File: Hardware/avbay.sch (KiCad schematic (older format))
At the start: 15 parts, among them P1 TERM_BLOCK_2.54MM_2POS, P2 CONN_6, P3 TERM_BLOCK_2.54MM_12POS, P4 TERM_BLOCK_2.54MM_2POS, P5 TERM_BLOCK_2.54MM_2POS, SW1 SW_PUSH, SW2 SW_PUSH

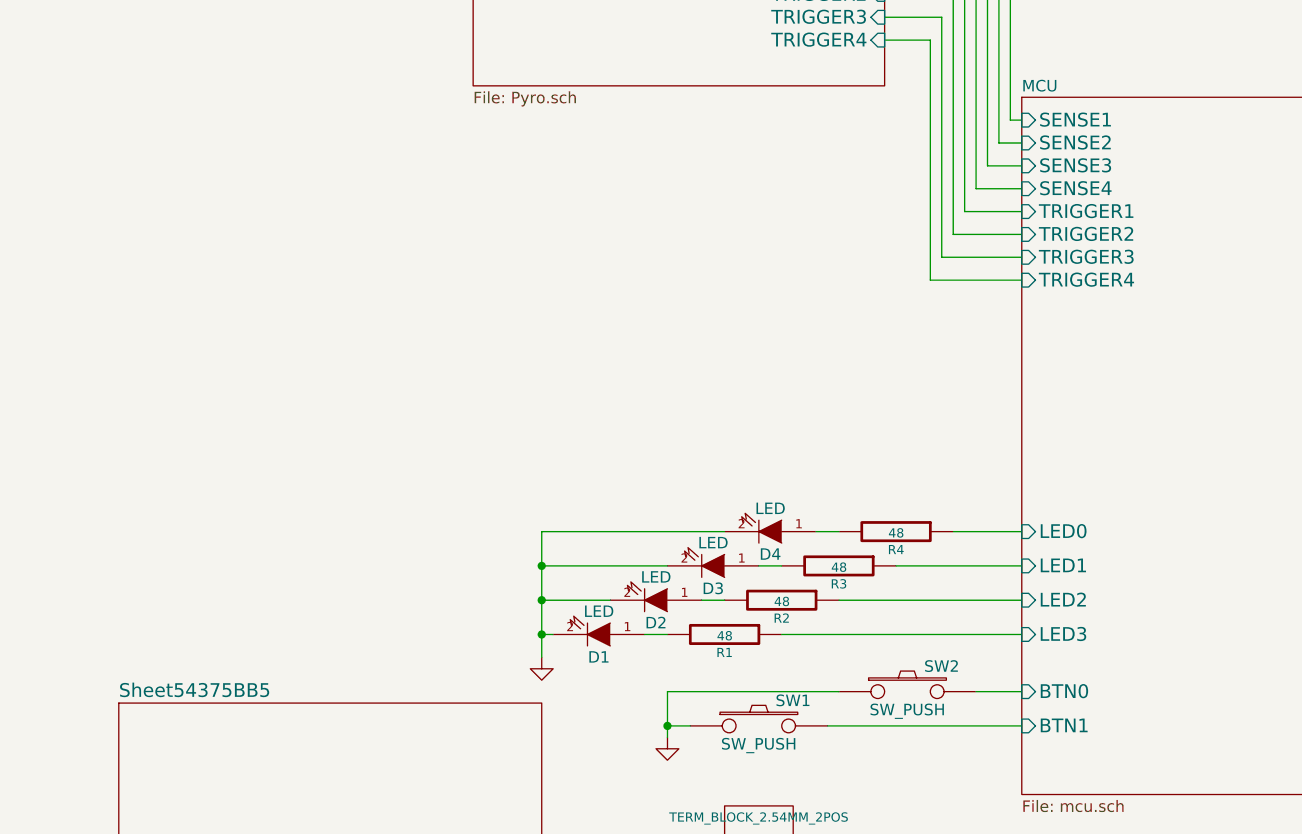
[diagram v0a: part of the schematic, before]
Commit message: Added sensors and sensor passives
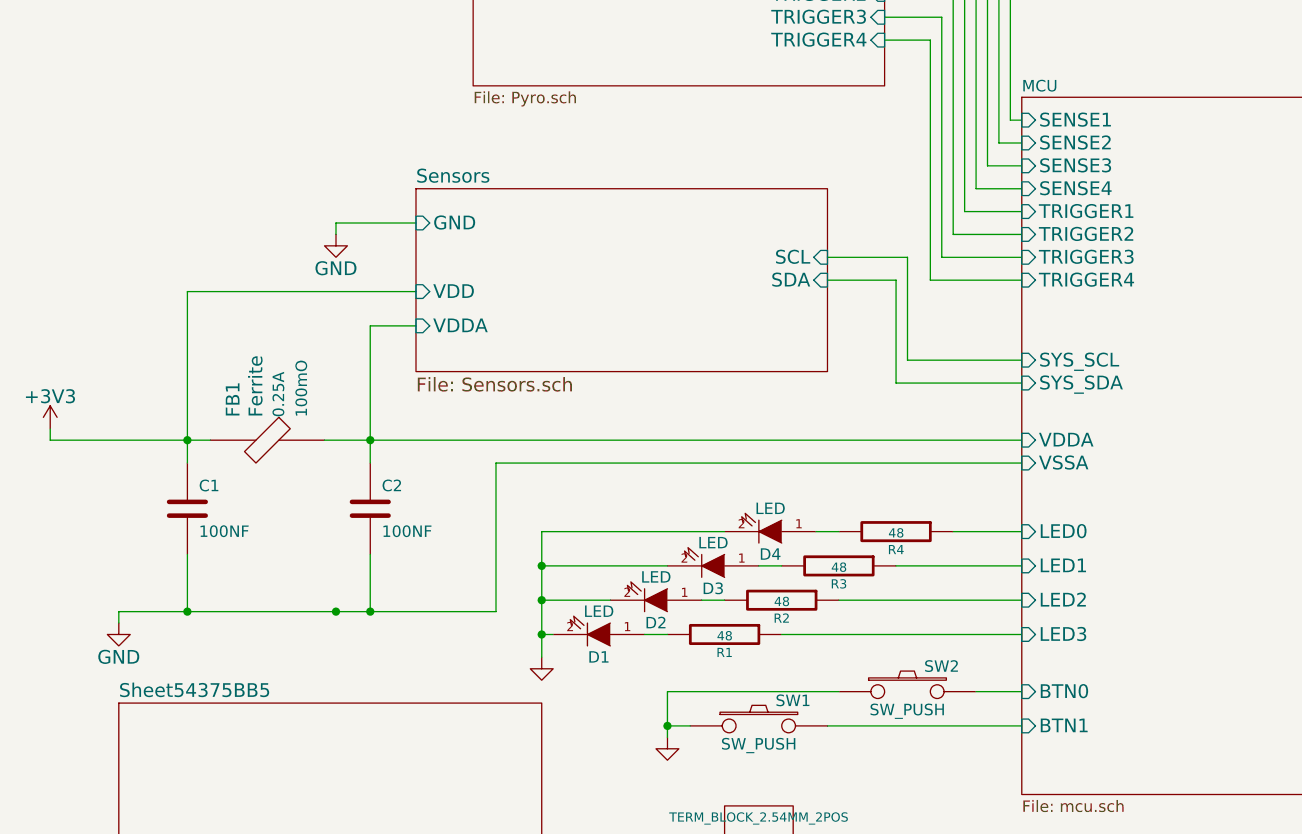
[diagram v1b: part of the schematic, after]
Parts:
- added C1, C2: 100NF, symbol C
- added FB1: Ferrite, symbol Ferrite
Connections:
- net labels added: +3V3
- wire segments 95 -> 116

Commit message: Roughed out PCB layout
Known issues:
- SW_PUSH holes too small. New footprint needed
- Sensor footprints are completely wrong.
- Regulator footprints might not be correct.

Tasks:
- Place passives according to schematic (especially
  with decoupling capacitors.
- Condense layout as much as possible for
  smallest board size
- Route board
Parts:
- removed P3: TERM_BLOCK_2.54MM_12POS, symbol TERM_BLOCK_2.54MM_12POS
- removed P4, P5: TERM_BLOCK_2.54MM_2POS, symbol TERM_BLOCK_2.54MM_2POS
- removed SW1: SW_PUSH, Discret:SW_PUSH_SMALL, symbol SW_PUSH
- added P3: TERM_BLOCK_2.54MM_8POS, Socket_Strips:Socket_Strip_Straight_1x08, symbol TERM_BLOCK_2.54MM_8POS
- added P4, P5: TERM_BLOCK_2.54MM_5POS, Socket_Strips:Socket_Strip_Straight_1x05, symbol TERM_BLOCK_2.54MM_5POS
- C1, C2: footprint (none) -> Capacitors_SMD:C_0805_HandSoldering
- FB1: footprint (none) -> SMD_Packages:SMD-1206
- P1: footprint (none) -> Socket_Strips:Socket_Strip_Straight_1x02
- P2: footprint Pin_Headers:Pin_Header_Angled_1x06 -> Socket_Strips:Socket_Strip_Angled_1x06
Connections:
- wire segments 116 -> 126
- no-connect marks 0 -> 4

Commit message: Began routing
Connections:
- no-connect marks 4 -> 5

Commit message: Finished routing.
Board awaiting review
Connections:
- net +3V3 is gone; now on net 3V3: C1.1, FB1.1, P3.5 (P5)
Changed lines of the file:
@@
-$EndComp
-$Comp
-L +3V3 #PWR09
-U 1 1 54C47AF6
-P 650 4050
-F 0 "#PWR09" H 650 3900 60  0001 C CNN
-F 1 "+3V3" H 650 4190 60  0000 C CNN
-F 2 "" H 650 4050 60  0000 C CNN
-F 3 "" H 650 4050 60  0000 C CNN
-	1    650  4050
-	1    0    0    -1
 $EndComp
 $Comp
@@
 $EndSheet
 $Comp
-L GND #PWR010
+L GND #PWR09
 U 1 1 54C502C9
 P 1900 3200
-F 0 "#PWR010" H 1900 2950 60  0001 C CNN
+F 0 "#PWR09" H 1900 2950 60  0001 C CNN
 F 1 "GND" H 1900 3050 60  0000 C CNN
 F 2 "" H 1900 3200 60  0000 C CNN
@@
 $EndComp
 $Comp
-L GND #PWR011
+L GND #PWR010
 U 1 1 5437EF10
 P 9200 5050
-F 0 "#PWR011" H 9200 5050 30  0001 C CNN
+F 0 "#PWR010" H 9200 5050 30  0001 C CNN
 F 1 "GND" H 9200 4980 30  0001 C CNN
 F 2 "" H 9200 5050 60  0000 C CNN
@@
 $EndComp
 $Comp
-L +3V3 #PWR012
-U 1 1 54C4EBE1
-P 7600 5700
-F 0 "#PWR012" H 7600 5550 60  0001 C CNN
-F 1 "+3V3" H 7600 5840 60  0000 C CNN
-F 2 "" H 7600 5700 60  0000 C CNN
-F 3 "" H 7600 5700 60  0000 C CNN
-	1    7600 5700
-	1    0    0    -1
-$EndComp
-$Comp
-L +5V #PWR013
+L +5V #PWR011
 U 1 1 54C4EC96
 P 7700 5700
-F 0 "#PWR013" H 7700 5550 60  0001 C CNN
+F 0 "#PWR011" H 7700 5550 60  0001 C CNN
 F 1 "+5V" H 7700 5840 60  0000 C CNN
 F 2 "" H 7700 5700 60  0000 C CNN
@@
 $EndComp
 $Comp
-L GND #PWR014
+L GND #PWR012
 U 1 1 54C501F1
 P 8300 5800
-F 0 "#PWR014" H 8300 5800 30  0001 C CNN
+F 0 "#PWR012" H 8300 5800 30  0001 C CNN
 F 1 "GND" H 8300 5730 30  0001 C CNN
 F 2 "" H 8300 5800 60  0000 C CNN
@@
 $EndComp
 $Comp
-L PWR_FLAG #FLG015
+L PWR_FLAG #FLG013
 U 1 1 54CB18F4
 P 3200 6300
-F 0 "#FLG015" H 3200 6395 30  0001 C CNN
+F 0 "#FLG013" H 3200 6395 30  0001 C CNN
 F 1 "PWR_FLAG" H 3200 6480 30  0000 C CNN
 F 2 "" H 3200 6300 60  0000 C CNN
@@
 $EndComp
 $Comp
-L PWR_FLAG #FLG016
+L PWR_FLAG #FLG014
 U 1 1 54CB23F4
 P 1900 4100
-F 0 "#FLG016" H 1900 4195 30  0001 C CNN
+F 0 "#FLG014" H 1900 4195 30  0001 C CNN
 F 1 "PWR_FLAG" H 1900 4280 30  0000 C CNN
 F 2 "" H 1900 4100 60  0000 C CNN
@@
 Connection ~ 3200 6300
 $Comp
-L PWR_FLAG #FLG017
+L PWR_FLAG #FLG015
 U 1 1 54CB3533
 P 4200 6300
-F 0 "#FLG017" H 4200 6395 30  0001 C CNN
+F 0 "#FLG015" H 4200 6395 30  0001 C CNN
 F 1 "PWR_FLAG" H 4200 6480 30  0000 C CNN
 F 2 "" H 4200 6300 60  0000 C CNN
@@
 	4900 5350 4700 5350
 NoConn ~ 4700 5350
+$Comp
+L 3V3 #PWR016
+U 1 1 54CB4FB3
+P 650 4050
+F 0 "#PWR016" H 650 4150 40  0001 C CNN
+F 1 "3V3" H 650 4175 40  0000 C CNN
+F 2 "" H 650 4050 60  0000 C CNN
+F 3 "" H 650 4050 60  0000 C CNN
+	1    650  4050
+	1    0    0    -1
+$EndComp
+$Comp
+L 3V3 #PWR017
+U 1 1 54CB65F0
+P 7600 5700
+F 0 "#PWR017" H 7600 5800 40  0001 C CNN
+F 1 "3V3" H 7600 5825 40  0000 C CNN
+F 2 "" H 7600 5700 60  0000 C CNN
+F 3 "" H 7600 5700 60  0000 C CNN
+	1    7600 5700
+	1    0    0    -1
+$EndComp
 $EndSCHEMATC

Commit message: Fixed footprints for tecminal blocks
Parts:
- P1: footprint Socket_Strips:Socket_Strip_Straight_1x02 -> Local:TERM_BLOCK_2
- P2: footprint Socket_Strips:Socket_Strip_Angled_1x06 -> Socket_Strips:Socket_Strip_Straight_1x06
- P4, P5: footprint Socket_Strips:Socket_Strip_Straight_1x05 -> Local:TERM_BLOCK_5
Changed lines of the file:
@@
 F 0 "P2" V 8350 2700 60  0000 C CNN
 F 1 "CONN_6" V 8450 2700 60  0000 C CNN
-F 2 "Socket_Strips:Socket_Strip_Angled_1x06" H 8400 2700 60  0001 C CNN
+F 2 "Socket_Strips:Socket_Strip_Straight_1x06" H 8400 2700 60  0001 C CNN
 F 3 "" H 8400 2700 60  0000 C CNN
 	1    8400 2700
@@
 F 0 "P4" V 9550 3450 60  0000 C CNN
 F 1 "TERM_BLOCK_2.54MM_5POS" V 9650 3450 60  0000 C CNN
-F 2 "Socket_Strips:Socket_Strip_Straight_1x05" H 9600 3450 60  0001 C CNN
+F 2 "Local:TERM_BLOCK_5" H 9600 3450 60  0001 C CNN
 F 3 "" H 9600 3450 60  0000 C CNN
 	1    9600 3450
@@
 F 0 "P5" V 9550 4700 60  0000 C CNN
 F 1 "TERM_BLOCK_2.54MM_5POS" V 9650 4700 60  0000 C CNN
-F 2 "Socket_Strips:Socket_Strip_Straight_1x05" H 9600 4700 60  0001 C CNN
+F 2 "Local:TERM_BLOCK_5" H 9600 4700 60  0001 C CNN
 F 3 "" H 9600 4700 60  0000 C CNN
 	1    9600 4700
@@
 F 0 "P1" V 3700 5800 40  0000 C CNN
 F 1 "TERM_BLOCK_2.54MM_2POS" V 3800 5800 40  0000 C CNN
-F 2 "Socket_Strips:Socket_Strip_Straight_1x02" H 3750 5800 60  0001 C CNN
+F 2 "Local:TERM_BLOCK_2" H 3750 5800 60  0001 C CNN
 F 3 "" H 3750 5800 60  0000 C CNN
 	1    3750 5800

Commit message: Finished schematic work. Began footprints
Began assigning footprints for R2
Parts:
- added D5: DIODE, Diodes_SMD:Diode-MELF_Handsoldering, symbol DIODE
- added Q5: NPN, Housings_SOT-23_SOT-143_TSOT-6:SOT-23_Handsoldering, symbol NPN
- added R16: 180, Resistors_SMD:R_0805_HandSoldering, symbol R
- added SP1: SPEAKER, symbol SPEAKER
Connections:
- net 3V3: now also D5.2 (K), SP1.1
- net GND: now also Q5.1 (E)
- net MCU/GPIO4: now also R16.1
- new net: Q5.2 (B), R16.2
- new net: D5.1 (A), Q5.3 (C), SP1.2
- no-connect marks 5 -> 2
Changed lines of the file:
@@
 F20 "GPIO4" I R 6900 5000 60
 F21 "GPIO5" I R 6900 5100 60
-F22 "GPIO6" I R 6900 5200 60
-F23 "GPIO7" I R 6900 5300 60
+F22 "GPIO6" I L 4900 3550 60
+F23 "GPIO7" I L 4900 3650 60
 F24 "SENSE1" I L 4900 2700 60
 F25 "SENSE2" I L 4900 2800 60
@@
 F5 "SDA" I R 4050 3400 60
 F6 "VDD" I L 2250 3450 60
+F7 "ACCEL_INT_1" I R 4050 3600 60
+F8 "ACCEL_INT_2" I R 4050 3700 60
 $EndSheet
 $Comp
@@
 	0    1    1    0
 $EndComp
-NoConn ~ 7900 5300
-NoConn ~ 7800 5200
 NoConn ~ 7700 5100
 $Comp
@@
 	0    -1   1    0
 $EndComp
-NoConn ~ 7600 5000
 Wire Wire Line
 	8050 3250 8050 3500
@@
 	7900 5700 7900 5800
 Wire Wire Line
-	7800 5700 8300 5700
+	7800 5700 8500 5700
 Wire Wire Line
 	7700 5800 7700 5700
@@
 	8300 5700 8300 5800
 Wire Wire Line
-	6900 5300 7900 5300
-Wire Wire Line
-	6900 5200 7800 5200
-Wire Wire Line
-	6900 5100 7700 5100
-Wire Wire Line
-	6900 5000 7600 5000
+	6900 5000 8550 5000
 Wire Wire Line
 	7500 4900 7500 5800
@@
 	1    0    0    -1
 $EndComp
+$Comp
+L NPN Q5
+U 1 1 550518B1
+P 9300 5800
+F 0 "Q5" H 9300 5650 50  0000 R CNN
+F 1 "NPN" H 9300 5950 50  0000 R CNN
+F 2 "Housings_SOT-23_SOT-143_TSOT-6:SOT-23_Handsoldering" H 9300 5800 60  0001 C CNN
+F 3 "" H 9300 5800 60  0000 C CNN
+	1    9300 5800
+	1    0    0    -1
+$EndComp
+Wire Wire Line
+	8500 5700 8500 6150
+Wire Wire Line
+	8500 6150 9400 6150
+Wire Wire Line
+	9400 6150 9400 6000
+Connection ~ 8300 5700
+Wire Wire Line
+	9100 5800 8550 5800
+$Comp
+L SPEAKER SP1
+U 1 1 55051E92
+P 10500 5400
+F 0 "SP1" H 10400 5650 50  0000 C CNN
+F 1 "SPEAKER" H 10400 5150 50  0000 C CNN
+F 2 "" H 10500 5400 60  0001 C CNN
+F 3 "" H 10500 5400 60  0000 C CNN
+	1    10500 5400
+	1    0    0    -1
+$EndComp
+$Comp
+L DIODE D5
+U 1 1 55051ECF
+P 9900 5400
+F 0 "D5" H 9900 5500 50  0000 C CNN
+F 1 "DIODE" H 9900 5300 50  0000 C CNN
+F 2 "Diodes_SMD:Diode-MELF_Handsoldering" H 9900 5400 60  0001 C CNN
+F 3 "" H 9900 5400 60  0000 C CNN
+	1    9900 5400
+	0    -1   -1   0
+$EndComp
+$Comp
+L 3V3 #PWR018
+U 1 1 55051F3E
+P 10200 5100
+F 0 "#PWR018" H 10200 5200 40  0001 C CNN
+F 1 "3V3" H 10200 5225 40  0000 C CNN
+F 2 "" H 10200 5100 60  0000 C CNN
+F 3 "" H 10200 5100 60  0000 C CNN
+	1    10200 5100
+	1    0    0    -1
+$EndComp
+Wire Wire Line
+	10200 5100 10200 5300
+Wire Wire Line
+	9900 5200 10200 5200
+Connection ~ 10200 5200
+Wire Wire Line
+	9400 5600 10200 5600
+Wire Wire Line
+	10200 5600 10200 5500
+Connection ~ 9900 5600
+$Comp
+L R R16
+U 1 1 550554F1
+P 8550 5350
+F 0 "R16" V 8630 5350 50  0000 C CNN
+F 1 "180" V 8557 5351 50  0000 C CNN
+F 2 "Resistors_SMD:R_0805_HandSoldering" V 8480 5350 30  0001 C CNN
+F 3 "" H 8550 5350 30  0000 C CNN
+	1    8550 5350
+	1    0    0    -1
+$EndComp
+Wire Wire Line
+	8550 5000 8550 5100
+Wire Wire Line
+	8550 5800 8550 5600
+Wire Wire Line
+	6900 5100 7700 5100
+Wire Wire Line
+	4900 3550 4300 3550
+Wire Wire Line
+	4300 3550 4300 3600
+Wire Wire Line
+	4300 3600 4050 3600
+Wire Wire Line
+	4900 3650 4300 3650
+Wire Wire Line
+	4300 3650 4300 3700
+Wire Wire Line
+	4300 3700 4050 3700
 $EndSCHEMATC

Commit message: Ready to begin laying out and routing
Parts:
- SP1: footprint (none) -> Local:CBT-07427
- SW2: footprint Discret:SW_PUSH_SMALL -> Local:SW_SMD
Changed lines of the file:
@@
 F 0 "SW2" H 4550 5310 50  0000 C CNN
 F 1 "SW_PUSH" H 4400 5120 50  0000 C CNN
-F 2 "Discret:SW_PUSH_SMALL" H 4400 5200 60  0001 C CNN
+F 2 "Local:SW_SMD" H 4400 5200 60  0001 C CNN
 F 3 "" H 4400 5200 60  0000 C CNN
 	1    4400 5200
@@
 F 0 "SP1" H 10400 5650 50  0000 C CNN
 F 1 "SPEAKER" H 10400 5150 50  0000 C CNN
-F 2 "" H 10500 5400 60  0001 C CNN
+F 2 "Local:CBT-07427" H 10500 5400 60  0001 C CNN
 F 3 "" H 10500 5400 60  0000 C CNN
 	1    10500 5400
